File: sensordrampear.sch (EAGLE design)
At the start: 23 parts, among them IC1 PCA9534D, IC2 MCP601SN

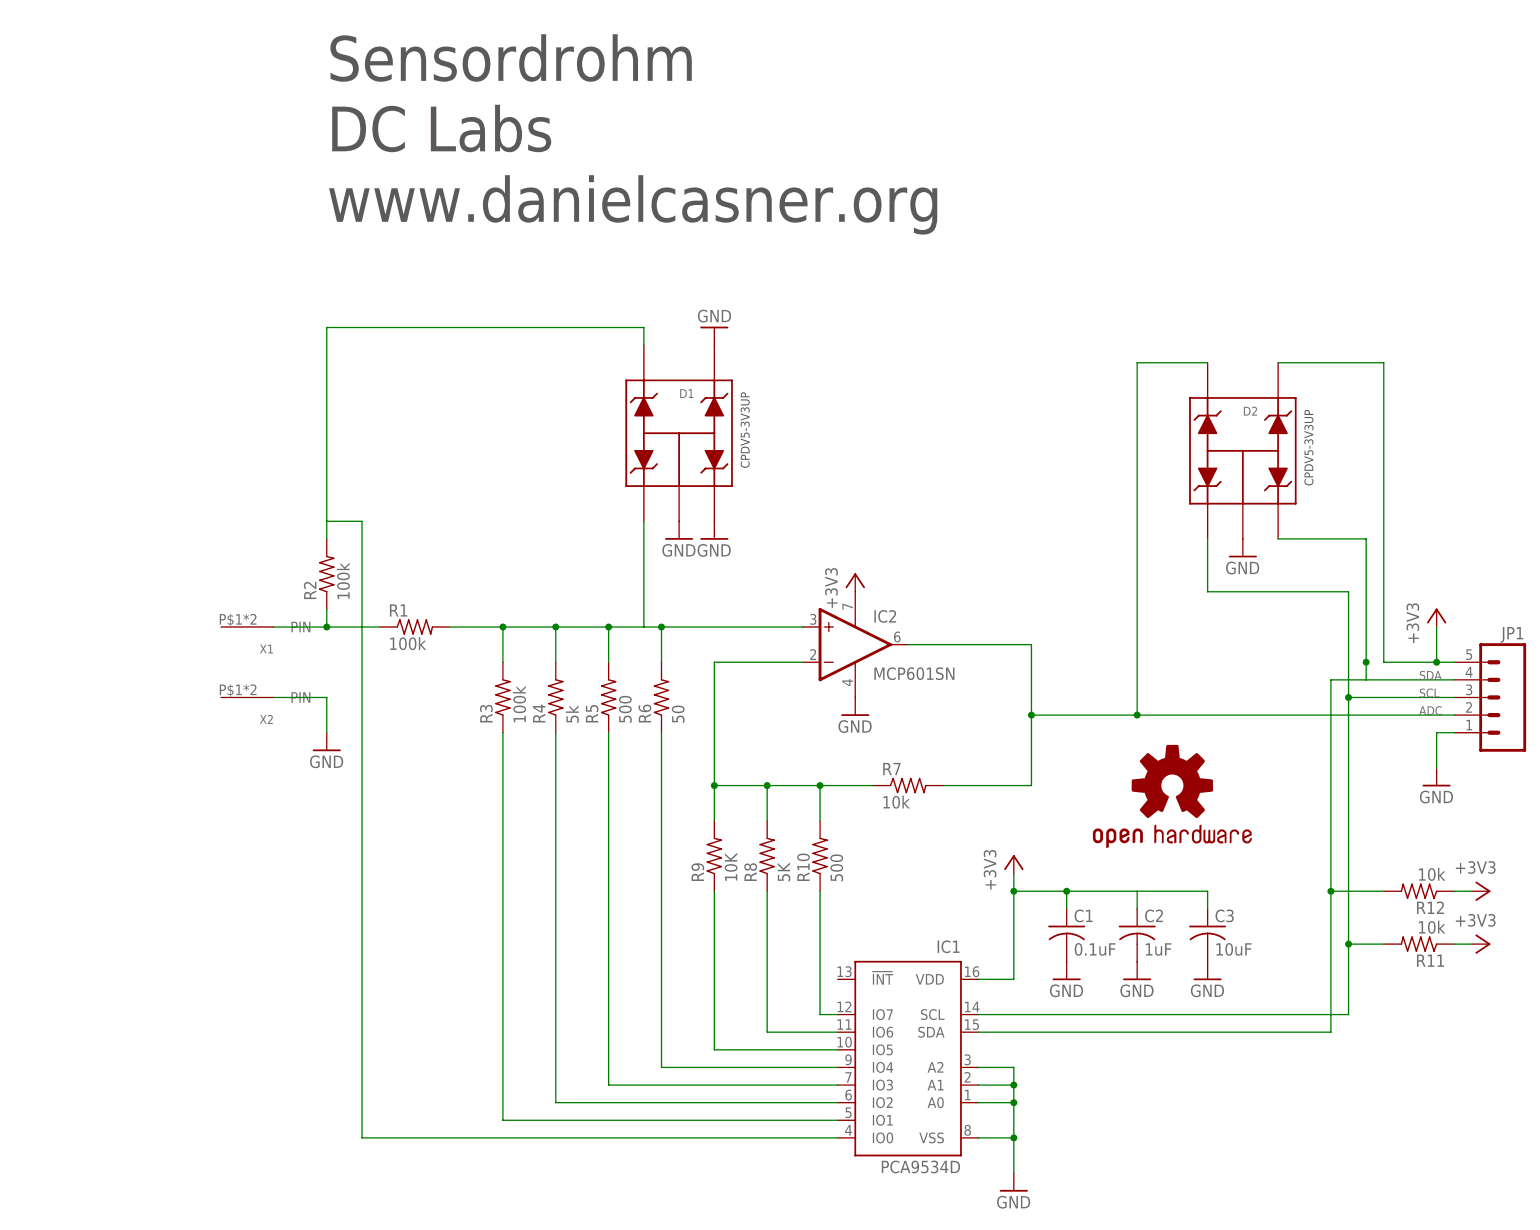
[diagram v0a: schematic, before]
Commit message: Add SensordrAMPEAR and sensor drone audio jack schematics.
More rough plans for Sensordrone accessories.
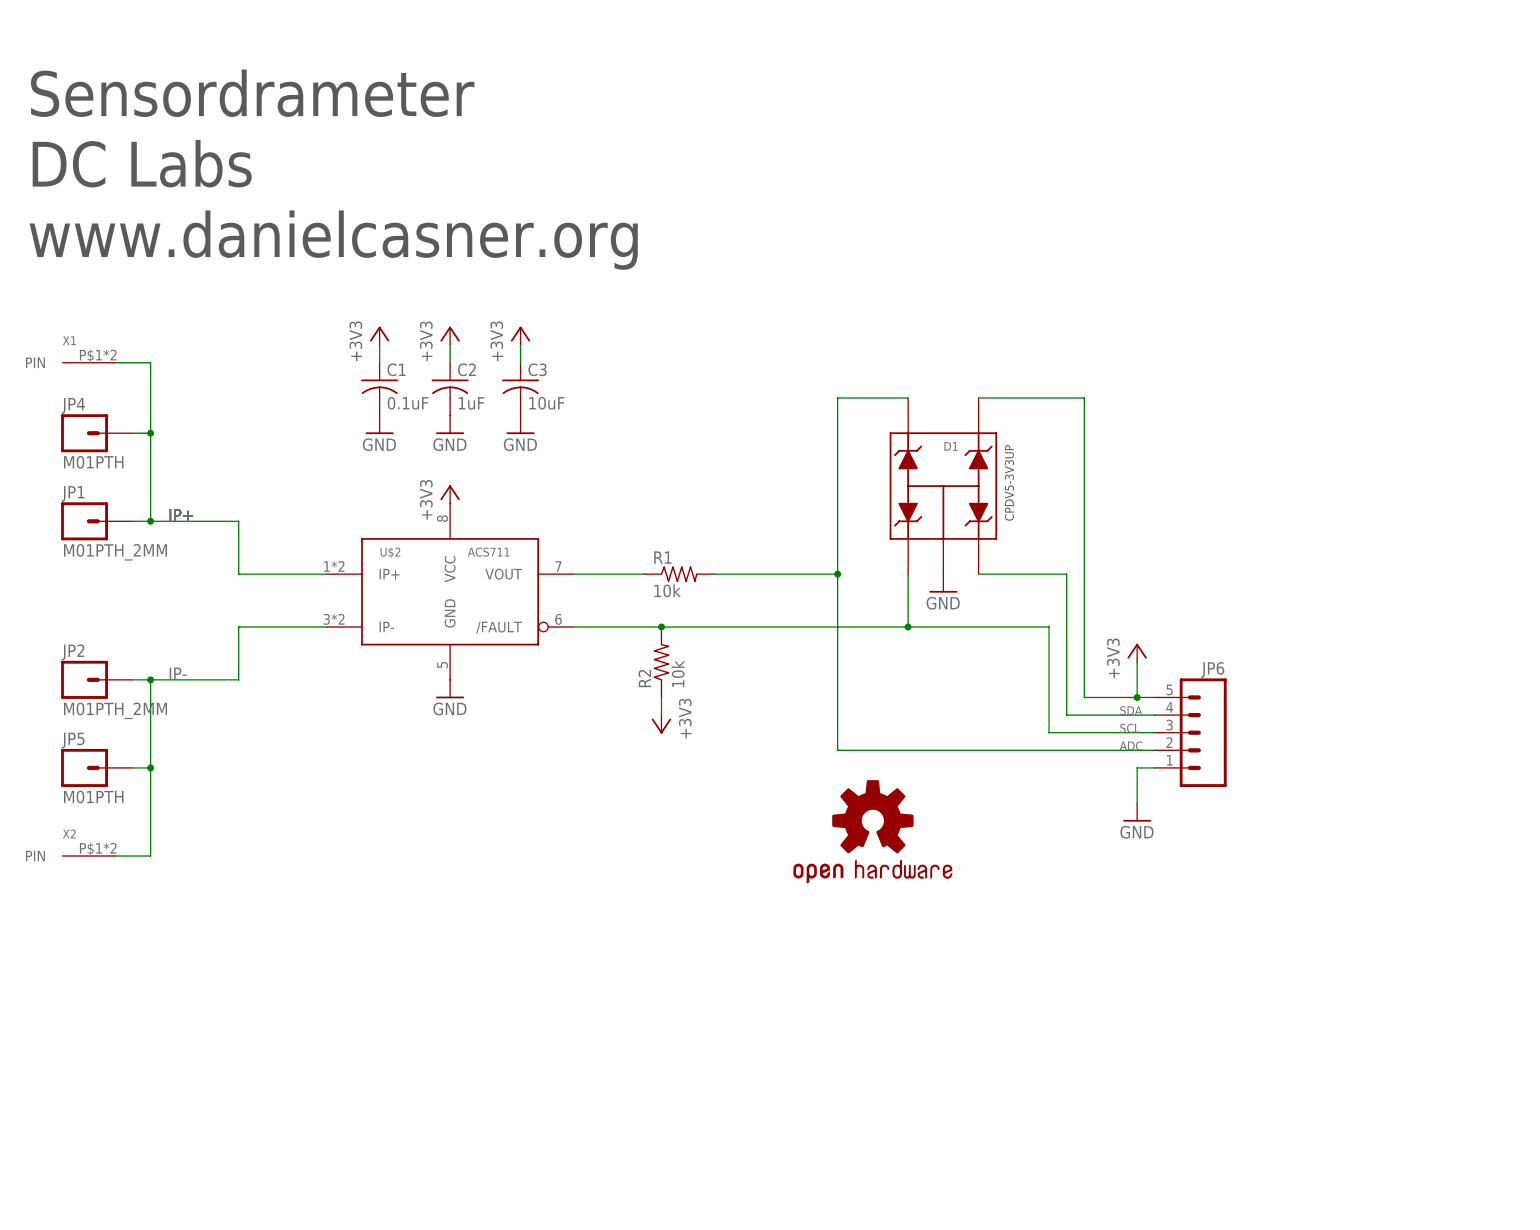
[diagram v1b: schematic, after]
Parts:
- removed D2: CPDV5-3V3UP, DMM:CPDV5
- removed IC1: PCA9534D, micro-philips:PCA9534D
- removed IC2: MCP601SN, linear:MCP601SN
- removed R10, R5: 500, rcl:R-US_R0402
- removed R11, R12, R7: 10k, rcl:R-US_R0402
- removed R3: 100k, rcl:R-US_R0402
- removed R4: 5k, rcl:R-US_R0402
- removed R6: 50, rcl:R-US_R0402
- removed R8: 5K, rcl:R-US_R0402
- removed R9: 10K, rcl:R-US_R0402
- added JP2: M01PTH_2MM, SparkFun:M01PTH_2MM
- added JP4, JP5: M01PTH, SparkFun:M01PTH
- added JP6: (no value), SparkFun-Connectors:M05PTH_LONGPADS
- added U$2: ACS711, DMM:ACS711
- JP1: value (none) -> M01PTH_2MM; device SparkFun-Connectors:M05PTH_LONGPADS -> SparkFun:M01PTH_2MM
- R1, R2: value 100k -> 10k
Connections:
- removed net N$1: R1.1, R2.1
- removed net N$10: IC1.IO5, R9.1
- removed net N$11: IC1.IO6, R8.1
- removed net N$14: IC1.IO7, R10.1
- removed net N$2: D1.P$1, IC2.+IN, R1.2, R3.2, R4.2, R5.2, R6.2
- removed net N$4: IC2.-IN, R10.2, R7.1, R8.2, R9.2
- removed net N$5: D1.P$5, IC1.IO0, R2.2
- removed net N$6: IC1.IO1, R3.1
- removed net N$7: IC1.IO2, R4.1
- removed net N$8: IC1.IO3, R5.1
- removed net N$9: IC1.IO4, R6.1
- new net IP+: JP1.1, JP4.1, U$2.IP+, X1.PIN
- new net IP-: JP2.1, JP5.1, U$2.IP-, X2.PIN
- new net N$3: R1.1, U$2.VOUT
- net +3V3: now also D1.P$4, JP6.5, R2.1, U$2.VCC; no longer D2.P$4, IC1.VDD, IC2.V+, JP1.5, R11.1, R12.1
- net ADC: now also D1.P$5, JP6.2, R1.2; no longer D2.P$5, IC2.OUT, JP1.2, R7.2
- net GND: now also JP6.1, U$2.GND; no longer D1.P$3, D1.P$4, D2.P$2, IC1.A0, IC1.A1, IC1.A2, IC1.VSS, IC2.V-, JP1.1
- net SCL: now also D1.P$1, JP6.3, R2.2, U$2./FAULT; no longer D2.P$1, IC1.SCL, JP1.3, R11.2
- net SDA: now also D1.P$3, JP6.4; no longer D2.P$3, IC1.SDA, JP1.4, R12.2
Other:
- note added: "Sensordrameter"
- note removed: "Sensordrohm"
- moved on the sheet: C1, C2, C3, D1, R1, R2, X1, X2
